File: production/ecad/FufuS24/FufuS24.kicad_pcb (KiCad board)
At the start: 4 copper layers, 120 x 120 mm, 0 parts

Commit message: efab "we layed out"
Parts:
- added C1: 4.7uF, footprints:CAPC2012X94N, F.Cu at (180.7, 120.4)
- added C10: 1u, footprints:CAPC2012X94N, F.Cu at (146.3, 94.6)
- added C11: 100n, footprints:CAPC2012X94N, F.Cu at (146.3, 97.6)
- added C12: 100n, footprints:CAPC2012X94N, F.Cu at (146.3, 100.6)
- added C13: 100n, footprints:CAPC2012X94N, F.Cu at (150.7, 88.6)
- added C14: 100n, footprints:CAPC2012X94N, F.Cu at (150.7, 91.6)
- added C15: 100n, footprints:CAPC2012X94N, F.Cu at (150.7, 94.6)
- added C16: 100n, footprints:CAPC2012X94N, F.Cu at (150.7, 97.6)
- added C17: 10uF 25V, footprints:CAPC2012X94N, F.Cu at (121.0, 115.9)
- added C18: 0.1uF 63V, footprints:CAPC2012X94N, F.Cu at (158.8, 136.3)
- added C19: 100nF, footprints:CAPC2012X94N, F.Cu at (183.7, 120.4)
- added C2: 27p, footprints:CAPC2012X94N, F.Cu at (135.0, 102.2)
- added C20: 100nF, footprints:CAPC2012X94N, F.Cu at (186.7, 120.4)
- added C21: 10uF, footprints:CAPC2012X94N, F.Cu at (189.7, 120.4)
- added C22: 100nF, footprints:CAPC2012X94N, F.Cu at (181.6, 132.1)
- added C23: 10uF, footprints:CAPC2012X94N, F.Cu at (185.4, 132.1)
- added C24: 10uF, footprints:CAPC2012X94N, F.Cu at (189.5, 132.1)
- added C25: 10uF, footprints:CAPC2012X94N, F.Cu at (182.9, 135.9)
- added C26: 100nF, footprints:CAPC2012X94N, F.Cu at (183.9, 102.4)
- added C27: 4.7uF, footprints:CAPC2012X94N, F.Cu at (187.1, 135.9)
- added C28: 100nF, footprints:CAPC2012X94N, F.Cu at (192.4, 120.7)
- added C29: 10uF, footprints:CAPC2012X94N, F.Cu at (188.3, 96.4)
- added C3: 27p, footprints:CAPC2012X94N, F.Cu at (128.7, 102.2)
- added C30: 10uF, footprints:CAPC2012X94N, F.Cu at (188.3, 99.4)
- added C31: 10uF, footprints:CAPC2012X94N, F.Cu at (188.3, 102.4)
- added C32: 4.7uF, footprints:CAPC2012X94N, F.Cu at (188.3, 105.4)
- added C33: 100nF, footprints:CAPC2012X94N, F.Cu at (183.8, 97.8)
- added C34: 4.7uF, footprints:CAPC2012X94N, F.Cu at (175.5, 83.8)
- added C35: ECWF6754HL, footprints:CAPC2012X94N, F.Cu at (121.0, 121.9)
- added C36: 10uF, footprints:CAPC2012X94N, F.Cu at (183.7, 116.3)
- added C37: 10uF, footprints:CAPC2012X94N, F.Cu at (186.7, 116.3)
- added C38: 10uF, footprints:CAPC2012X94N, F.Cu at (175.5, 87.0)
- added C39: 100nF, footprints:CAPC2012X94N, F.Cu at (186.9, 63.0)
- added C4: 3.3 uF 275V, footprints:CAPC2012X94N, F.Cu at (121.0, 112.9)
- added C40: 100nF, footprints:CAPC2012X94N, F.Cu at (186.9, 66.0)
- added C41: 100nF, footprints:CAPC2012X94N, F.Cu at (186.9, 69.1)
- added C42: 100nF, footprints:CAPC2012X94N, F.Cu at (191.4, 63.0)
- added C43: 100nF, footprints:CAPC2012X94N, F.Cu at (191.4, 66.0)
- added C44: 100nF, footprints:CAPC2012X94N, F.Cu at (191.4, 69.1)
- added C45: 100nF, footprints:CAPC2012X94N, F.Cu at (195.9, 63.0)
- added C46: 100nF, footprints:CAPC2012X94N, F.Cu at (195.9, 66.0)
- added C47: 100nF, footprints:CAPC2012X94N, F.Cu at (195.9, 69.1)
- added C5: 100n, footprints:CAPC2012X94N, F.Cu at (143.3, 83.6)
- added C51: 0.1uF 63V, footprints:CAPC2012X94N, F.Cu at (121.0, 124.9)
- added C6: 100n, footprints:CAPC2012X94N, F.Cu at (141.8, 97.6)
- added C7: 100n, footprints:CAPC2012X94N, F.Cu at (141.8, 100.6)
- added C8: 1u, footprints:CAPC2012X94N, F.Cu at (146.3, 88.6)
- added C9: 100n, footprints:CAPC2012X94N, F.Cu at (146.3, 91.6)
- added D1: D_Schottky, footprints:ShocktyDiode0805, F.Cu at (187.2, 73.7)
- added D10: 150080GS75000, footprints:LED_GS75000_WRE, F.Cu at (93.1, 69.4)
- added D11: 150080GS75000, footprints:LED_GS75000_WRE, F.Cu at (93.1, 72.4)
- added D2: D_Schottky, footprints:ShocktyDiode0805, F.Cu at (187.2, 76.5)
- added D3: 150080GS75000, footprints:LED_GS75000_WRE, F.Cu at (197.2, 81.3)
- added D4: 150080GS75000, footprints:LED_GS75000_WRE, F.Cu at (197.2, 84.3)
- added D5: 150080GS75000, footprints:LED_GS75000_WRE, F.Cu at (197.2, 87.3)
- added D6: 150080GS75000, footprints:LED_GS75000_WRE, F.Cu at (197.2, 90.3)
- added D7: 150080GS75000, footprints:LED_GS75000_WRE, F.Cu at (197.2, 93.3)
- added IC1: NLVPCA9535EDTR2G, footprints:SOP65P640X120-24N, F.Cu at (123.4, 90.4)
- added J1: Conn_01x02, footprints:CONN2_710002_WRE, F.Cu at (97.8, 144.8)
- added J10: 691137710002, footprints:CONN2_710002_WRE, F.Cu at (134.6, 144.8)
- added J12: 691137710002, footprints:CONN2_710002_WRE, F.Cu at (85.1, 90.2)
- added J13: 5033950410, footprints:MOLEX4_CON_5033950410, F.Cu at (83.4, 106.1)
- added J2: Conn_01x02, footprints:CON_5025840270_MOL, B.Cu at (88.9, 49.6)
- added J3: HDMI_A, footprints:HDMI_A, F.Cu at (161.8, 33.8)
- added J4: USB_B_Micro, footprints:USB_Micro, F.Cu at (179.2, 35.5)
- added J5: 691137710004, footprints:PWR_4POS, F.Cu at (97.9, 35.3)
- added J6: 5025840270, footprints:CON_5025840270_MOL, F.Cu at (111.8, 147.3)
- added J7: 691137710002, footprints:CONN2_710002_WRE, F.Cu at (167.6, 144.8)
- added J8: 691137710004, footprints:PWR_4POS, F.Cu at (85.1, 130.7)
- added J9: 5025840270, footprints:CON_5025840270_MOL, F.Cu at (124.0, 147.3)
- added L1: 10uH, footprints:INDPM120120X800N, F.Cu at (109.2, 129.5)
- added L2: 33uH, footprints:INDPM120120X800N, F.Cu at (171.4, 130.8)
- added L3: 12uH, footprints:0805Inductor, F.Cu at (167.9, 98.4)
- added L4: 33uH, footprints:INDPM120120X800N, F.Cu at (171.4, 116.2)
- added Q1: DMG2302UK-7, footprints:DMG2302UK-7_Footprint, F.Cu at (116.6, 102.5)
- added R1: 1k, footprints:RESC2012X60N, F.Cu at (131.2, 82.5)
- added R10: 64.9k, footprints:RESC2012X60N, F.Cu at (192.7, 112.6)
- added R11: 3.3k, footprints:RESC2012X60N, F.Cu at (129.9, 129.5)
- added R12: 110k, footprints:RESC2012X60N, F.Cu at (192.7, 115.6)
- added R13: 110k, footprints:RESC2012X60N, F.Cu at (193.4, 132.7)
- added R14: 10k, footprints:RESC2012X60N, F.Cu at (193.4, 135.6)
- added R15: 64.9k, footprints:RESC2012X60N, F.Cu at (197.2, 132.7)
- added R16: 64.9k, footprints:RESC2012X60N, F.Cu at (197.9, 97.4)
- added R17: 110k, footprints:RESC2012X60N, F.Cu at (193.7, 97.4)
- added R18: 27k, footprints:RESC2012X60N, F.Cu at (193.7, 100.3)
- added R19: 4.7k, footprints:RESC2012X60N, F.Cu at (131.1, 90.9)
- added R2: DNF, footprints:RESC2012X60N, F.Cu at (131.2, 85.5)
- added R20: 100, footprints:RESC2012X60N, F.Cu at (104.5, 110.1)
- added R21: 5.6, footprints:RESC2012X60N, F.Cu at (178.1, 44.5)
- added R22: 5.6, footprints:RESC2012X60N, F.Cu at (178.1, 47.4)
- added R23: 5.6, footprints:RESC2012X60N, F.Cu at (178.1, 50.3)
- added R24: 5.6, footprints:RESC2012X60N, F.Cu at (178.1, 53.2)
- added R25: 5.6, footprints:RESC2012X60N, F.Cu at (178.1, 56.2)
- added R26: 5.6, footprints:RESC2012X60N, F.Cu at (178.1, 59.1)
- added R27: 5.6, footprints:RESC2012X60N, F.Cu at (178.1, 62.0)
- added R28: 5.6, footprints:RESC2012X60N, F.Cu at (178.1, 65.0)
- added R29: 4.7k, footprints:RESC2012X60N, F.Cu at (131.1, 94.0)
- added R3: 27.4, footprints:RESC2012X60N, F.Cu at (131.2, 88.4)
- added R30: 500, footprints:RESC2012X60N, F.Cu at (104.5, 113.0)
- added R31: 4.7k, footprints:RESC2012X60N, F.Cu at (191.2, 81.5)
- added R32: 1.3k, footprints:RESC2012X60N, F.Cu at (191.2, 84.4)
- added R33: 909, footprints:RESC2012X60N, F.Cu at (191.2, 87.3)
- added R34: 200, footprints:RESC2012X60N, F.Cu at (191.2, 90.3)
- added R35: 30, footprints:RESC2012X60N, F.Cu at (191.4, 93.3)
- added R36: 7.32k, footprints:RESC2012X60N, F.Cu at (196.5, 117.5)
- added R38: 10k, footprints:RESC2012X60N, F.Cu at (197.5, 135.9)
- added R39: 10k, footprints:RESC2012X60N, F.Cu at (198.2, 100.6)
- added R4: 27.4, footprints:RESC2012X60N, F.Cu at (135.6, 82.5)
- added R40: 10k, footprints:RESC2012X60N, F.Cu at (196.5, 120.7)
- added R41: 1.75k, footprints:RESC2012X60N, F.Cu at (147.0, 82.2)
- added R42: 1.75k, footprints:RESC2012X60N, F.Cu at (147.0, 85.1)
- added R44: R_US, footprints:RESC2012X60N, F.Cu at (87.6, 60.6)
- added R45: R_US, footprints:RESC2012X60N, F.Cu at (87.6, 63.5)
- added R46: R_US, footprints:RESC2012X60N, F.Cu at (87.6, 66.4)
- added R5: 1k, footprints:RESC2012X60N, F.Cu at (131.8, 106.0)
- added R6: 330, footprints:RESC2012X60N, F.Cu at (121.0, 127.9)
- added R7: 16, footprints:RESC2012X60N, F.Cu at (121.0, 130.8)
- added R8: 10k, footprints:RESC2012X60N, F.Cu at (121.0, 133.8)
- added R9: 0.1 5W, footprints:RESC2012X60N, F.Cu at (121.0, 136.7)
- added TP1: 5014, footprints:TP_5014, F.Cu at (181.0, 75.0)
- added TP10: 5014, footprints:TP_5014, F.Cu at (196.2, 109.2)
- added TP11: 5014, footprints:TP_5014, F.Cu at (175.9, 98.4)
- added TP12: 5014, footprints:TP_5014, F.Cu at (195.6, 127.0)
- added TP13: 5014, footprints:TP_5014, F.Cu at (104.1, 100.2)
- added TP14: 5014, footprints:TP_5014, F.Cu at (104.1, 95.8)
- added TP2: 5014, footprints:TP_5014, F.Cu at (181.0, 79.4)
- added TP3: 5014, footprints:TP_5014, F.Cu at (181.0, 83.9)
- added TP4: 5014, footprints:TP_5014, F.Cu at (181.0, 88.4)
- added TP5: 5014, footprints:TP_5014, F.Cu at (181.0, 92.8)
- added TP6: 5014, footprints:TP_5014, F.Cu at (94.0, 52.1)
- added TP7: 5014, footprints:TP_5014, F.Cu at (94.0, 56.8)
- added TP8: 5014, footprints:TP_5014, F.Cu at (94.0, 61.5)
- added TP9: 5014, footprints:TP_5014, F.Cu at (135.9, 114.3)
- added U1: RP2040, footprints:RP2040_Footprint, F.Cu at (139.1, 90.5)
- added U10: TPD4E1U06DBVR, footprints:RP2040_Footprint, F.Cu at (169.2, 56.8)
- added U11: TPD4E1U06DBVR, footprints:TPD4E1U06DBVR_footprint, F.Cu at (185.4, 55.6)
- added U12: Pololu_DRV8711_Motor_Driver, footprints:POLOLU_36v4, B.Cu at (135.9, 42.1)
- added U2: W25Q128JVS, footprints:W25Q128JVSIM_footprint, F.Cu at (147.5, 77.5)
- added U3: TPD2E001DRLR, footprints:QFN-FCMOD_365R6FRDN_TEX, F.Cu at (168.9, 66.4)
- added U4: TPS785, footprints:DPAK114P990X239-6N, F.Cu at (167.0, 87.0)
- added U5: PLMR38020FDDAR, footprints:DDA0008E-MFG, F.Cu at (185.1, 110.5)
- added U6: PLMR38020FDDAR, footprints:DDA0008E-MFG, F.Cu at (186.1, 126.4)
- added U7: PLMR38020FDDAR, footprints:DDA0008E-MFG, F.Cu at (171.8, 105.4)
- added U8: ~, footprints:FOD3150_footprint, F.Cu at (154.9, 127.0)
- added U9: ~, footprints:IRFB4610PBF, F.Cu at (141.0, 123.7)
- added Y1: ~, footprints:XTAL_ABLS-12.000MHZ-B4-T, F.Cu at (131.8, 97.8)
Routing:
- net GNDREF: vias 0 -> 1
- net (no net): vias 4 -> 3

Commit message: efan part 2 laying out
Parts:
- J2, U12: moved to F.Cu
- moved R16 112.3 mm to (85.6, 98.3)
- moved R15 111.1 mm to (86.1, 131.2), turned to 180 degrees
- moved J12 109.6 mm to (194.6, 94.1)
- moved J8 109.0 mm to (194.1, 134.1)
- moved C28 107.5 mm to (85.1, 127.6)
- moved R10 106.9 mm to (85.9, 111.8)
- moved J2 106.6 mm to (191.0, 80.2)
- moved J13 105.2 mm to (188.6, 109.9)
- moved C41 104.8 mm to (82.3, 62.5)
- moved C44 104.8 mm to (86.8, 62.5)
- moved C32 104.3 mm to (84.6, 94.9), turned to 90 degrees
- moved R31 101.0 mm to (91.2, 67.5)
- moved D3 100.9 mm to (97.3, 67.5)
- moved R32 100.7 mm to (91.2, 72.8)
- moved D4 100.6 mm to (97.3, 72.8)
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
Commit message: Update FufuS24.kicad_pcb
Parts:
- moved C23 37.8 mm to (82.4, 120.8), turned to -90 degrees
- moved C20 37.1 mm to (132.8, 125.3)
- moved R10 36.1 mm to (116.7, 130.6), turned to 180 degrees
- moved U5 35.3 mm to (124.1, 126.9)
- moved C19 34.4 mm to (116.5, 125.7)
- moved C24 34.3 mm to (85.1, 120.8), turned to -90 degrees
- moved C1 33.8 mm to (113.7, 125.7)
- moved C25 30.8 mm to (88.0, 120.8), turned to -90 degrees
- moved TP10 27.5 mm to (117.6, 135.8)
- moved R40 26.6 mm to (124.1, 135.3), turned to 180 degrees
- moved C29 25.7 mm to (82.2, 93.2)
- moved C30 24.7 mm to (85.2, 93.3), turned to -90 degrees
- moved R36 23.5 mm to (128.1, 131.3), turned to 0 degrees
- moved R12 23.4 mm to (131.0, 134.2)
- moved R39 22.3 mm to (95.8, 106.6), turned to 180 degrees
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
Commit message: efan laying out
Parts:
- moved C34 32.3 mm to (101.9, 69.3)
- moved C38 32.3 mm to (113.5, 69.0)
- moved U4 32.3 mm to (107.7, 70.6)
- moved R38 7.32 mm to (89.4, 135.1)
- moved TP12 7.32 mm to (82.8, 135.4)
- moved C26 4.85 mm to (102.3, 92.3)
- moved C30 4.85 mm to (85.0, 88.4)
- moved C32 4.85 mm to (85.0, 93.5)
- moved C33 4.85 mm to (87.9, 93.5)
- moved R16 4.85 mm to (89.0, 98.2)
- moved R17 4.85 mm to (102.0, 100.9)
- moved R18 4.85 mm to (99.3, 98.1)
- moved R39 4.85 mm to (95.5, 101.8)
- moved TP11 4.85 mm to (84.6, 101.0)
- moved U7 4.85 mm to (95.5, 93.9)
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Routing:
- net GNDREF: track 0.00 -> 1.24 mm
- net Net-(U6-SW): track 0.00 -> 0.85 mm
- added copper zone on F.Cu, net (none)
- added copper zone on F.Cu, net +12V
- added copper zone on F.Cu, net +16V
- added copper zone on F.Cu, net +48V
- added copper zone on F.Cu, net GNDREF

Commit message: laying out
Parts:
- L3: footprint footprints:0805Inductor -> footprints:INDPM120120X800N
- moved C38 31.7 mm to (93.5, 93.6)
- moved U4 31.7 mm to (87.7, 95.2)
- moved C34 31.7 mm to (81.8, 93.9)
- moved IC1 17.6 mm to (133.1, 75.6)
- moved L3 17.1 mm to (111.5, 82.3)
- moved C33 15.6 mm to (103.5, 92.5)
- moved C32 15.6 mm to (100.5, 92.5)
- moved C29 15.4 mm to (97.4, 87.9)
- moved C26 15.4 mm to (117.7, 91.8)
- moved C30 15.4 mm to (100.4, 87.9)
- moved C31 15.4 mm to (103.1, 88.0)
- moved U7 15.4 mm to (110.9, 93.4)
- moved R17 15.4 mm to (117.4, 100.8)
- moved R18 15.4 mm to (114.7, 98.2), turned to 180 degrees
- moved R39 14.9 mm to (110.4, 101.1)
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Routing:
- net GNDREF: track 1.24 -> 142.3 mm
- net +48V: track 0.46 -> 55.4 mm
- net +12V: track 0.09 -> 52.4 mm
- net +5V: track 0.00 -> 35.1 mm
- net Net-(U7-PG): track 0.00 -> 11.5 mm
- net +16V: track 0.28 -> 10.9 mm
- net Net-(U6-PG): track 0.00 -> 5.81 mm
- net Net-(U5-PG): track 0.00 -> 5.77 mm
- net +3V3: track 0.00 -> 4.68 mm
- net Net-(D7-Pad2): track 0.00 -> 4.28 mm
- net Net-(D6-Pad2): track 0.00 -> 4.26 mm
- net Net-(D3-Pad2): track 0.00 -> 4.25 mm
- net Net-(D5-Pad2): track 0.00 -> 4.24 mm
- net Net-(D4-Pad2): track 0.00 -> 4.23 mm
- added copper zone on F.Cu, net +3.3V
- added copper zone on F.Cu, net +5V

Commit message: lAYOUT
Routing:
- net GNDREF: track 142.3 -> 20.4 mm, vias 1 -> 4
- net +48V: track 55.4 -> 4.80 mm, vias 0 -> 5
- net Net-(U6-PG): track 5.81 -> 27.2 mm, vias 0 -> 2
- net Net-(U6-SW): track 0.85 -> 10.5 mm
- net Net-(U5-BOOT): track 0.00 -> 5.94 mm
- net Net-(U6-RT_SYNC): track 0.00 -> 4.86 mm
- net GND: vias 0 -> 5
- net (no net): vias 3 -> 0
- added copper zone on In2.Cu, net GNDREF
- added copper zone on F.Cu, net Net-(U5-SW)
- added copper zone on F.Cu, net Net-(U6-FB)

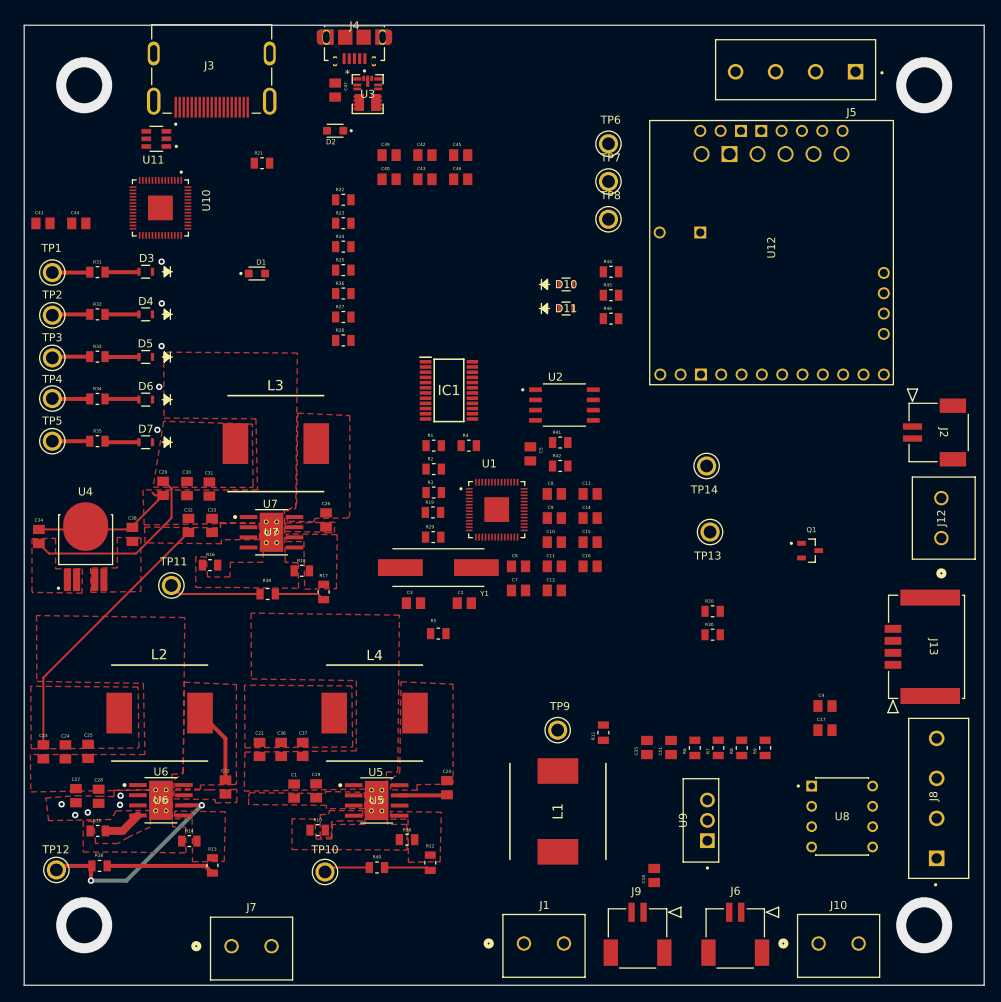
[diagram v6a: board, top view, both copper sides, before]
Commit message: Layout progress (no mcu or hdmi)
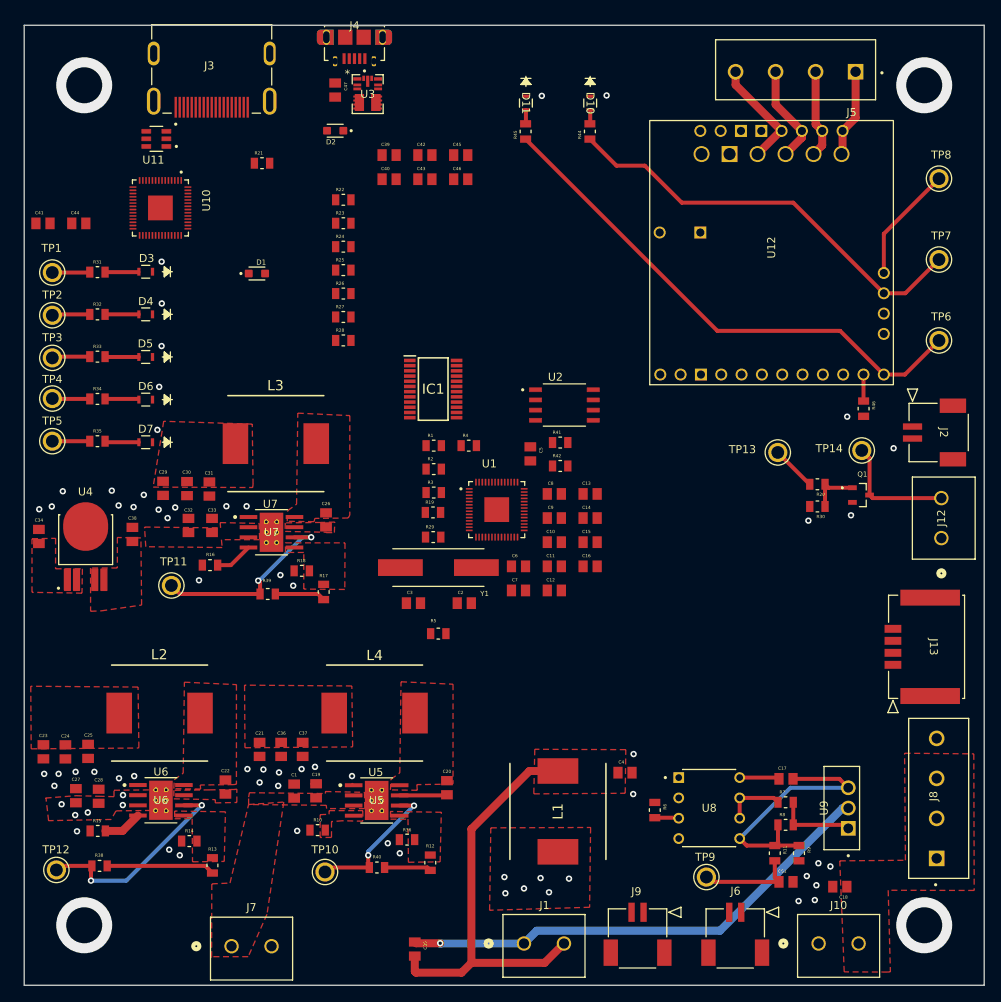
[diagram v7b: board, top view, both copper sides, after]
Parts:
- moved TP6 48.1 mm to (194.3, 69.4)
- moved TP7 42.5 mm to (194.3, 59.3)
- moved TP8 41.6 mm to (194.3, 49.2)
- moved C35 38.4 mm to (128.8, 145.5), turned to -90 degrees
- moved R46 33.5 mm to (184.9, 77.9), turned to -90 degrees
- moved C4 26.3 mm to (155.1, 123.4)
- moved R11 26.2 mm to (173.8, 133.5), turned to -90 degrees
- moved D11 26.2 mm to (142.7, 39.7), turned to -90 degrees
- moved TP9 26.1 mm to (165.3, 136.5)
- moved C18 23.2 mm to (181.9, 137.7), turned to 180 degrees
- moved R45 23.1 mm to (142.7, 43.3), turned to 90 degrees
- moved D10 22.9 mm to (150.8, 39.7), turned to -90 degrees
- moved C51 22.1 mm to (175.2, 137.1), turned to 0 degrees
- moved R30 20.7 mm to (179.2, 90.2), turned to 180 degrees
- moved R20 20.6 mm to (179.2, 87.4), turned to 180 degrees
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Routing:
- net Net-(U12-~FLT): track 0.00 -> 65.6 mm
- net Net-(J1-Pin_1): track 0.00 -> 61.4 mm, vias 0 -> 1
- net Net-(U12-~STALL): track 0.00 -> 53.4 mm
- net Net-(J1-Pin_2): track 0.00 -> 52.7 mm
- net /Induction Heating/VSS: track 0.00 -> 34.1 mm
- net +12V: track 52.4 -> 18.4 mm
- net +5V: track 35.1 -> 11.2 mm
- net GNDREF: track 20.4 -> 2.13 mm, vias 4 -> 54
- net Net-(Q1-D): track 0.00 -> 15.1 mm
- net Net-(U12-BEMF): track 0.00 -> 14.6 mm
- net Net-(U12-AOUT1): track 0.00 -> 14.0 mm
- net Net-(U7-PG): track 11.5 -> 24.3 mm, vias 0 -> 2
- net Net-(U12-AOUT2): track 0.00 -> 12.5 mm
- net Net-(C51-Pad1): track 0.00 -> 12.2 mm
- net Net-(U5-PG): track 5.77 -> 17.7 mm, vias 0 -> 2
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- added copper zone on F.Cu, net Net-(J1-Pin_2)
- added copper zone on F.Cu, net Net-(U5-FB)
- added copper zone on F.Cu, net Net-(U5-RT_SYNC)
- added copper zone on F.Cu, net Net-(U6-BOOT)
- added copper zone on F.Cu, net Net-(U6-SW)
- added copper zone on F.Cu, net Net-(U7-BOOT)
- added copper zone on F.Cu, net Net-(U7-FB)
- added copper zone on F.Cu, net Net-(U7-SW)
- removed copper zone on F.Cu, net (none)
- removed copper zone on F.Cu, net GNDREF

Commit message: Staring MCU routing
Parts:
- U10: footprint footprints:RP2040_Footprint -> footprints:TPD4E1U06DBVR_footprint
- moved R4 47.8 mm to (175.1, 109.4)
- moved R3 47.6 mm to (175.1, 106.7)
- moved R42 32.9 mm to (175.8, 101.0), turned to -90 degrees
- moved R41 32.1 mm to (173.0, 101.0), turned to -90 degrees
- moved C13 26.9 mm to (164.7, 111.5)
- moved C39 26.5 mm to (99.2, 47.7)
- moved C40 26.5 mm to (99.2, 50.7)
- moved C42 26.5 mm to (103.6, 47.7)
- moved C43 26.5 mm to (103.6, 50.7)
- moved C45 26.5 mm to (108.1, 47.7)
- moved C46 26.5 mm to (108.1, 50.7)
- moved C16 26.5 mm to (164.6, 120.2)
- moved C15 26.4 mm to (164.4, 117.2)
- moved C14 26.2 mm to (164.4, 114.0)
- moved D1 25.3 mm to (87.3, 48.3)
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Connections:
- C10 pad 1: +3V3 -> +3.3V
- C11 pad 1: +3V3 -> +3.3V
- C12 pad 1: +3V3 -> +3.3V
- C13 pad 1: +3V3 -> +3.3V
- C14 pad 1: +3V3 -> +3.3V
- C15 pad 1: +3V3 -> +3.3V
- C16 pad 1: +3V3 -> +3.3V
- C5 pad 1: +3V3 -> +3.3V
- C9 pad 1: +3V3 -> +3.3V
- R2 pad 2: +3V3 -> +3.3V
- U1 pad 1: +3V3 -> +3.3V
- U1 pad 10: +3V3 -> +3.3V
- U1 pad 22: +3V3 -> +3.3V
- U1 pad 33: +3V3 -> +3.3V
- U1 pad 42: +3V3 -> +3.3V
- U1 pad 43: +3V3 -> +3.3V
- U1 pad 44: +3V3 -> +3.3V
- U1 pad 48: +3V3 -> +3.3V
- U1 pad 49: +3V3 -> +3.3V
- U2 pad 8: +3V3 -> +3.3V
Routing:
- net +3.3V: track 0.00 -> 33.1 mm, vias 0 -> 2
- net Net-(U1-VREG_VOUT): track 0.00 -> 8.06 mm
- net Net-(Q1-D): track 15.1 -> 16.7 mm
